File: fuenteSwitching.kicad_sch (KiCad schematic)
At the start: 19 parts, among them J1 Conn_01x02_Pin, J2 Conn_01x02_Pin, J3 Screw_Terminal_01x02, Q1 BD139, Q2 BD140, Q3 BD139, Q4 BD140, Q5 IRF3710PBF, Q6 IRF3710PBF, U1 LM311, U2 LM311

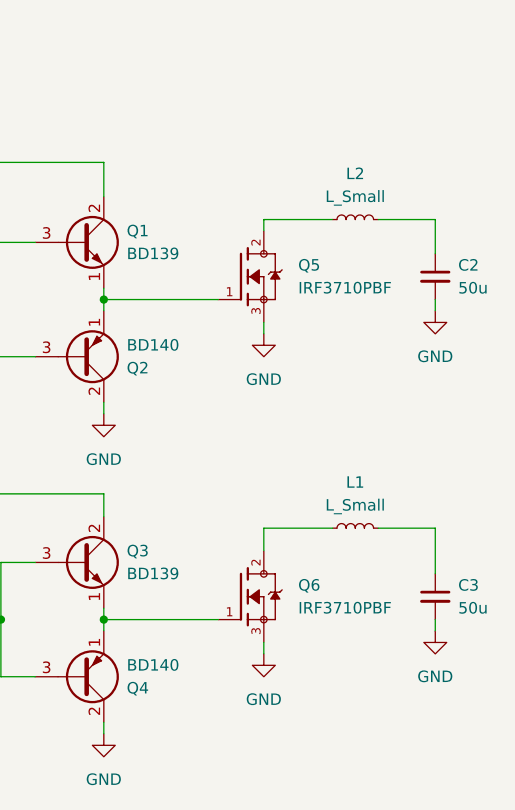
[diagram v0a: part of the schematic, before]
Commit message: Simulacion pwm OK
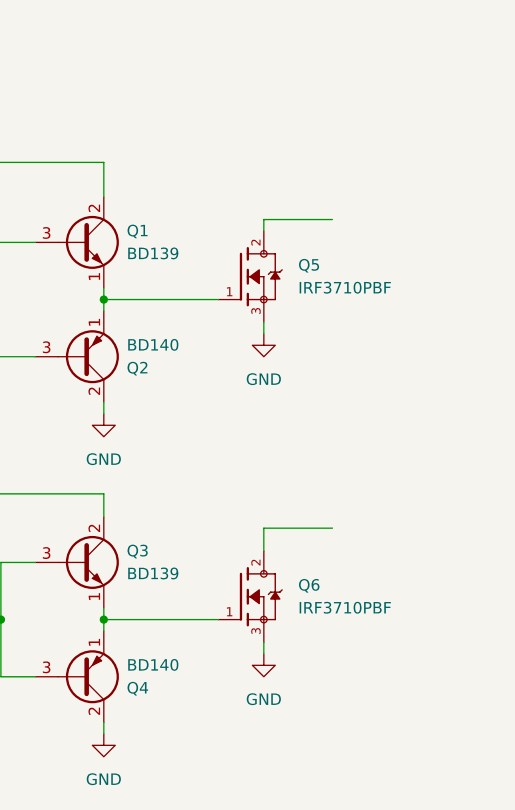
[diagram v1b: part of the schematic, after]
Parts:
- removed C2, C3: 50u, Capacitor_THT:C_Disc_D4.7mm_W2.5mm_P5.00mm, symbol Device:C_Small
- removed L1, L2: L_Small, symbol Device:L_Small
